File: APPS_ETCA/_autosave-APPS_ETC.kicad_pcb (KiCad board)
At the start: 2 copper layers, 81.3 x 85.7 mm, 21 parts, among them P1 DTM1312PC12PDR008, U1 NUCLEO-L432KC, U2 MCP6004, U6 LM7805_TO220, U8 LM7809_TO220

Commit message: pcb debugged
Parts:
- moved C4 4.67 mm to (216.5, 117.9)
- moved FS-2 APPS/ETC Board 4.58 mm to (228.0, 57.1)
- moved R5 0.63 mm to (224.2, 120.4)
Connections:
- C4 pad 1: /CANH -> +5V
- C4 pad 2: /CANL -> GND
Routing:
- net +5V: track 155.7 -> 159.7 mm, vias 6 -> 8
- net GND: track 398.7 -> 401.7 mm

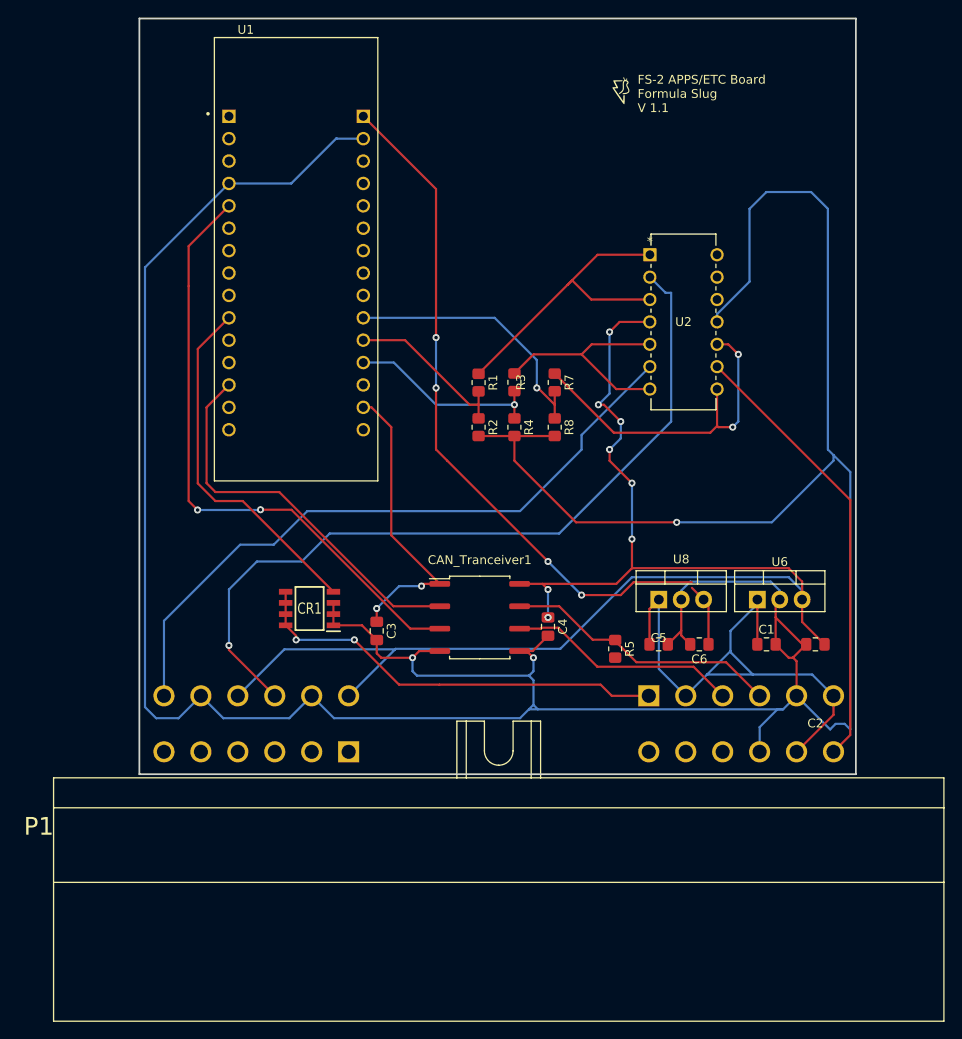
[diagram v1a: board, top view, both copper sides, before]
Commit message: added ground plane
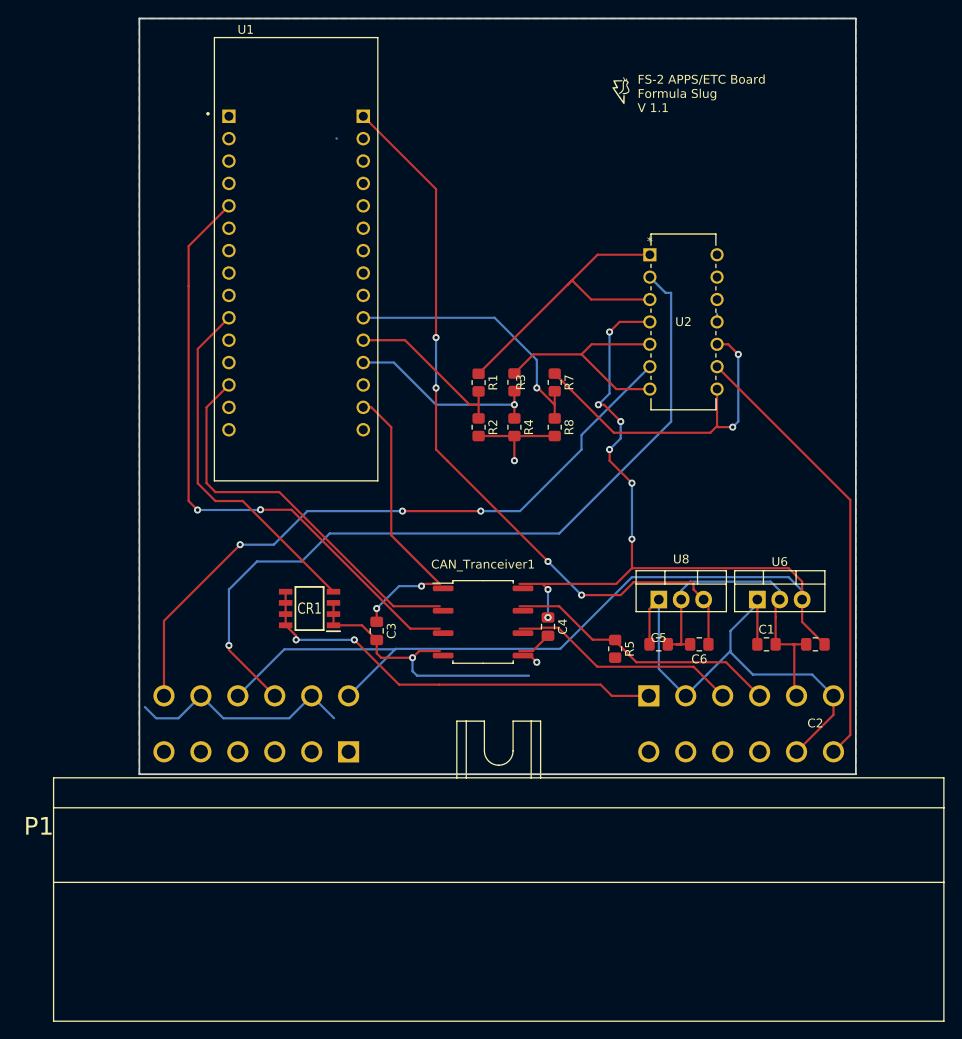
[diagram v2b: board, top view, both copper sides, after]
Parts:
- moved CAN_Tranceiver1 0.63 mm to (209.2, 117.3)
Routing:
- net GND: track 401.7 -> 115.6 mm
- net +12V: track 64.7 -> 59.5 mm
- net +9V: track 84.9 -> 85.5 mm
- net /OUT2: vias 0 -> 3
- added copper zone on B.Cu, net GND
